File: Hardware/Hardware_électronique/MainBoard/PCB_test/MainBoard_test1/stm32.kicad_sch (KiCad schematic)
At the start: 1 part, among them U1 STM32H735IGTx

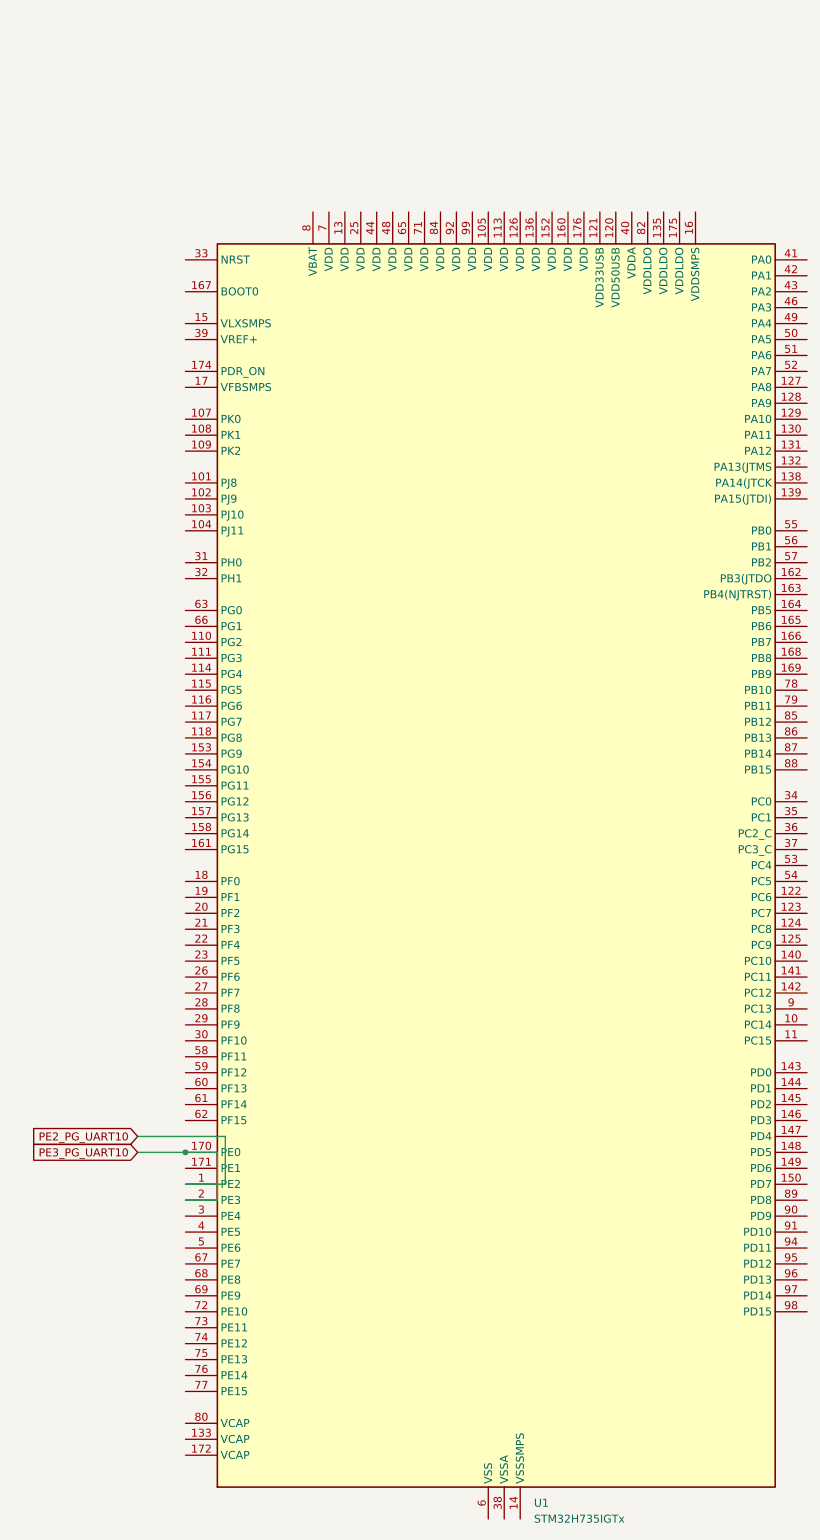
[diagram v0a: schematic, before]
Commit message: Adding motor board
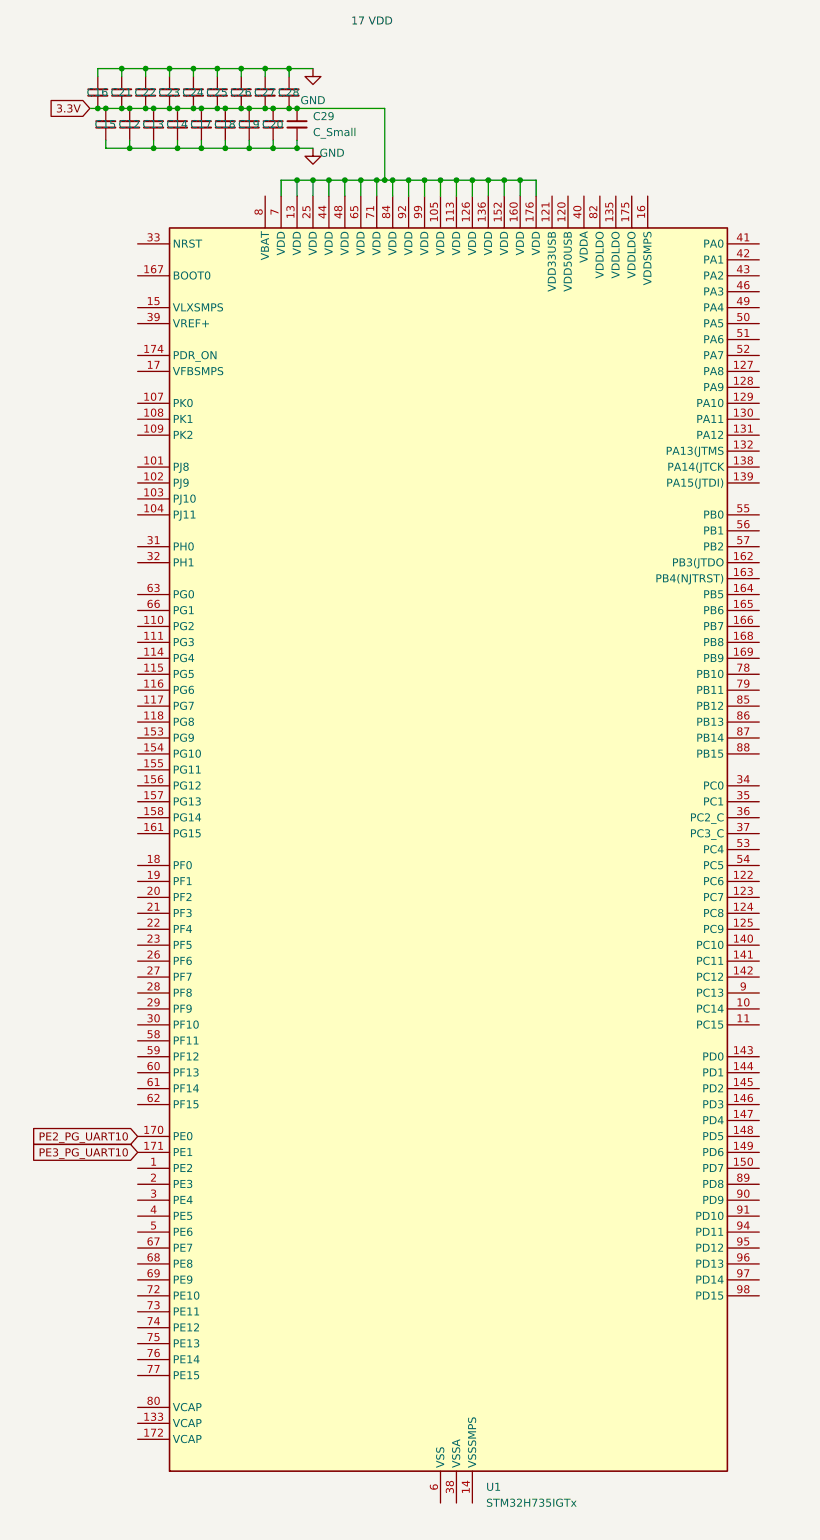
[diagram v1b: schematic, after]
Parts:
- added C12, C13, C14, C15, C16, C17, C18, C19, C20, C21, C22, C23, C24, C25, C26, C27, C28: 100n, symbol Device:C_Small
- added C29: C_Small, symbol Device:C_Small
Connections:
- net PE2_PG_UART10: now also U1.170 (PE0); no longer U1.1 (PE2)
- net PE3_PG_UART10: now also U1.171 (PE1); no longer U1.170 (PE0), U1.2 (PE3)
- net 3.3V: now reaches U1.105 (VDD)
- net 3.3V: now also U1.113 (VDD), U1.126 (VDD), U1.13 (VDD), U1.136 (VDD), U1.152 (VDD), U1.160 (VDD), U1.176 (VDD), U1.25 (VDD), U1.44 (VDD), U1.48 (VDD), U1.65 (VDD), U1.7 (VDD), U1.71 (VDD), U1.84 (VDD), U1.92 (VDD), U1.99 (VDD), C12.1, C13.1, C14.1, C15.1, C16.2, C17.1, C18.1, C19.1, C20.1, C21.2, C22.2, C23.2, C24.2, C25.2, C26.2, C27.2, C28.2, C29.1
- new net GND: C12.2, C13.2, C14.2, C15.2, C16.1, C17.2, C18.2, C19.2, C20.2, C21.1, C22.1, C23.1, C24.1, C25.1, C26.1, C27.1, C28.1, C29.2
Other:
- note added: "17 VDD"
- moved on the sheet: U1

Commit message: ey
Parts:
- added C30, C31, C32, C33: 10n, Capacitor_SMD:C_0402_1005Metric, symbol Device:C_Small
- added C34: 1u, Capacitor_SMD:C_0603_1608Metric_Pad1.08x0.95mm_HandSolder, symbol Device:C_Small
- added C35, C36: 100n, Capacitor_SMD:C_0402_1005Metric, symbol Device:C_Small
- added D18, D19, D20, D21: Blue LED, LED_SMD:LED_0603_1608Metric, symbol Device:LED
- added J2: Conn_ST_STDC14, Connector_PinHeader_1.27mm:PinHeader_2x07_P1.27mm_Vertical_SMD, symbol Connector:Conn_ST_STDC14
- added L3: 39n, Inductor_SMD:L_0603_1608Metric, symbol Device:L_Small
- added R12, R13, R14, R15, R16, R17, R18, R19: 10k, Resistor_SMD:R_0402_1005Metric, symbol Device:R_Small
- added R20, R21, R22, R23: 390, Resistor_SMD:R_0402_1005Metric, symbol Device:R_Small
- added SW1, SW2, SW3, SW4: SW_Push, Custom:435451019820, symbol Switch:SW_Push
- C29: value C_Small -> 10u
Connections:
- net GND: now also C16.2, C21.2, C22.2, C23.2, C24.2, C25.2, C26.2, C27.2, C28.2, U1.100 (VSS), U1.106 (VSS), U1.112 (VSS), U1.119 (VSS), U1.12 (VSS), U1.134 (VSS), U1.137 (VSS), U1.14 (VSSSMPS), U1.151 (VSS), U1.159 (VSS), U1.173 (VSS), U1.24 (VSS), U1.38 (VSSA), U1.45 (VSS), U1.47 (VSS), U1.6 (VSS), U1.64 (VSS), U1.70 (VSS), U1.81 (VSS), U1.83 (VSS), U1.93 (VSS), C30.1, C31.1, C32.1, C33.1, C34.2, C35.2, C36.2, J2.11 (GNDDetect), J2.5 (GND), J2.7 (GND), R20.2, R21.2, R22.2, R23.2, SW1.2, SW2.2, SW3.2, SW4.2; no longer C16.1, C21.1, C22.1, C23.1, C24.1, C25.1, C26.1, C27.1, C28.1
- net RX2: now reaches U1.148 (PD5)
- net TX2: now reaches U1.149 (PD6)
- net NRST: now reaches U1.33 (NRST)
- net NRST: now also C30.2, J2.12 (~{RST}), R12.2
- net +3.3VA: now reaches U1.40 (VDDA)
- net +3.3VA: now also C34.1, C35.1, C36.1, L3.2
- net TX3: now reaches U1.78 (PB10)
- net RX3: now reaches U1.79 (PB11)
- net +3.3V: now reaches U1.8 (VBAT)
- net +3.3V: now also C12.1, C13.1, C14.1, C15.1, C16.1, C17.1, C18.1, C19.1, C20.1, C21.1, C22.1, C23.1, C24.1, C25.1, C26.1, C27.1, C28.1, C29.1, U1.105 (VDD), U1.113 (VDD), U1.126 (VDD), U1.13 (VDD), U1.136 (VDD), U1.152 (VDD), U1.160 (VDD), U1.176 (VDD), U1.25 (VDD), U1.44 (VDD), U1.48 (VDD), U1.65 (VDD), U1.7 (VDD), U1.71 (VDD), U1.84 (VDD), U1.92 (VDD), U1.99 (VDD), J2.3 (VCC), L3.1, R16.2, R17.2, R18.2, R19.2
- net RX5: now reaches U1.85 (PB12)
- net TX5: now reaches U1.86 (PB13)
- net TX1: now reaches U1.87 (PB14)
- net RX1: now reaches U1.88 (PB15)
- removed net 3.3V: C12.1, C13.1, C14.1, C15.1, C16.2, C17.1, C18.1, C19.1, C20.1, C21.2, C22.2, C23.2, C24.2, C25.2, C26.2, C27.2, C28.2, C29.1, U1.105 (VDD), U1.113 (VDD), U1.126 (VDD), U1.13 (VDD), U1.136 (VDD), U1.152 (VDD), U1.160 (VDD), U1.176 (VDD), U1.25 (VDD), U1.44 (VDD), U1.48 (VDD), U1.65 (VDD), U1.7 (VDD), U1.71 (VDD), U1.84 (VDD), U1.92 (VDD), U1.99 (VDD)
- new net: R14.1, R18.1, SW3.1
- new net: D20.1 (K), R22.1
- new net: D21.1 (K), R23.1
- new net: R13.1, R17.1, SW2.1
- new net: R12.1, R16.1, SW1.1
- new net: D18.1 (K), R20.1
- new net: R15.1, R19.1, SW4.1
- new net: D19.1 (K), R21.1
- new net SWCLK: J2.6 (JCLK/SWCLK)
- new net SWDIO: J2.4 (JTMS/SWDIO)
- new net SWO: J2.8 (JTDO/SWO)
- new net USR_BTN_1: C31.2, R13.2
- new net USR_BTN_2: C32.2, R14.2
- new net USR_BTN_3: C33.2, R15.2
- new net USR_LED_1: D18.2 (A)
- new net USR_LED_2: D19.2 (A)
- new net USR_LED_3: D20.2 (A)
- new net USR_LED_4: D21.2 (A)
- new net VCP_RX: J2.13 (VCP_RX)
- new net VCP_TX: J2.14 (VCP_TX)
- no-connect marks 0 -> 16
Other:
- note added: "Buttons Configure uC for pull-up on user buttons"
- note added: "LEDS"
- note added: "ST-Link"
- moved on the sheet: C12, C13, C14, C15, C17, C18, C19, C20, C29

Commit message: commitment
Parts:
- added C37: 10u, Capacitor_SMD:C_0603_1608Metric_Pad1.08x0.95mm_HandSolder, symbol Device:C_Polarized
- added C38: 22u, Capacitor_SMD:C_0603_1608Metric_Pad1.08x0.95mm_HandSolder, symbol Device:C_Polarized
- added C39: 100n, Capacitor_SMD:C_0402_1005Metric, symbol Device:C_Small
- added D1, D2, D3, D4, D5, D6, D7, D8, D9: ESD7C5.0DT5G, Package_TO_SOT_SMD:SOT-416, symbol Power_Protection:RCLAMP0582B
- added LIDAR1, UART1, UART2, UART3, UART4, UART5, UART6, UART7, UART8: Conn_01x04_Male, Connector_JST:JST_XH_B4B-XH-A_1x04_P2.50mm_Vertical, symbol Connector:Conn_01x04_Male
- added TP2, TP5: TestPoint, TestPoint:TestPoint_Pad_D2.0mm, symbol Connector:TestPoint
- added U4: AZ1117-3.3, Package_TO_SOT_SMD:SOT-223-3_TabPin2, symbol Regulator_Linear:AZ1117-3.3
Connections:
- net +3.3V: now also C38.1, TP5.1, U4.2 (VO)
- net +3.3VA: now also U1.39 (VREF+)
- net GND: now also C37.2, C38.2, C39.1, D1.3 (A), D2.3 (A), D3.3 (A), D4.3 (A), D5.3 (A), D6.3 (A), D7.3 (A), D8.3 (A), D9.3 (A), LIDAR1.4 (Pin_4), U4.1 (GND), UART1.4 (Pin_4), UART2.4 (Pin_4), UART3.4 (Pin_4), UART4.4 (Pin_4), UART5.4 (Pin_4), UART6.4 (Pin_4), UART7.4 (Pin_4), UART8.4 (Pin_4)
- net NRST: now also C39.2
- net RX1: now also D1.2 (K2), UART1.3 (Pin_3)
- net RX2: now also D5.2 (K2), UART5.3 (Pin_3)
- net RX3: now also D2.2 (K2), UART2.3 (Pin_3)
- net RX5: now also D4.2 (K2), UART4.3 (Pin_3)
- net TX1: now also D1.1 (K1), UART1.2 (Pin_2)
- net TX2: now also D5.1 (K1), UART5.2 (Pin_2)
- net TX3: now also D2.1 (K1), UART2.2 (Pin_2)
- net TX5: now also D4.1 (K1), UART4.2 (Pin_2)
- net RXtoRPI: now reaches U1.1 (PE2)
- net TX8: now reaches U1.101 (PJ8)
- net TX8: now also D8.1 (K1), UART8.2 (Pin_2)
- net RX8: now reaches U1.102 (PJ9)
- net RX8: now also D8.2 (K2), UART8.3 (Pin_3)
- net TX6: now reaches U1.122 (PC6)
- net TX6: now also D6.1 (K1), UART6.2 (Pin_2)
- net RX6: now reaches U1.123 (PC7)
- net RX6: now also D6.2 (K2), UART6.3 (Pin_3)
- net RX4: now reaches U1.130 (PA11)
- net RX4: now also D3.2 (K2), UART3.3 (Pin_3)
- net TX4: now reaches U1.131 (PA12)
- net TX4: now also D3.1 (K1), UART3.2 (Pin_2)
- net TXtoRPI: now reaches U1.2 (PE3)
- net RX7: now reaches U1.67 (PE7)
- net RX7: now also D7.2 (K2), UART7.3 (Pin_3)
- net TX7: now reaches U1.68 (PE8)
- net TX7: now also D7.1 (K1), UART7.2 (Pin_2)
- net RX_Lidar: now reaches U1.97 (PD14)
- net RX_Lidar: now also D9.2 (K2), LIDAR1.3 (Pin_3)
- net TX_Lidar: now reaches U1.98 (PD15)
- net TX_Lidar: now also D9.1 (K1), LIDAR1.2 (Pin_2)
- net PE2_PG_UART10: no longer names the net of U1.170 (PE0)
- net PE3_PG_UART10: no longer names the net of U1.171 (PE1)
- new net +5V: C37.1, TP2.1, U4.3 (VI)
- new net VBUS: LIDAR1.1 (Pin_1), UART1.1 (Pin_1), UART2.1 (Pin_1), UART3.1 (Pin_1), UART4.1 (Pin_1), UART5.1 (Pin_1), UART6.1 (Pin_1), UART7.1 (Pin_1), UART8.1 (Pin_1)
- no-connect marks 16 -> 13
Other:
- moved on the sheet: C12, C13, C14, C15, C16, C17, C18, C19, C20, C21, C22, C23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

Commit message: hey
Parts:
- added C40: 100n, symbol Device:C_Small
- added C41: 100n, Capacitor_SMD:C_0402_1005Metric, symbol Device:C_Small
- added C42, C43, C44: 2.2u, symbol Device:C_Small
- added C45, C46, C47: 1u, Capacitor_SMD:C_0603_1608Metric_Pad1.08x0.95mm_HandSolder, symbol Device:C_Small
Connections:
- net USR_BTN_3 is gone; now on net BOOT0: C33.2, R15.2
- net +3.3V: now also U1.121 (VDD33USB), U1.135 (VDDLDO), U1.175 (VDDLDO), U1.82 (VDDLDO), C40.1, C45.1, C46.1, C47.1
- net +5V: now also U1.120 (VDD50USB), C41.1
- net GND: now also C40.2, C41.2, C42.2, C43.2, C44.2, C45.2, C46.2, C47.2
- net SWCLK: now also U1.138 (PA14(JTCK)
- net SWDIO: now also U1.132 (PA13(JTMS)
- net SWO: now also U1.162 (PB3(JTDO)
- net USR_BTN_1: now also U1.163 (PB4(NJTRST))
- net USR_BTN_2: now also U1.164 (PB5)
- net at U1.133 (VCAP): now also C43.1
- net BOOT0: now reaches U1.167 (BOOT0)
- net at U1.172 (VCAP): now also C44.1
- net at U1.80 (VCAP): now also C42.1
- no-connect marks 13 -> 100
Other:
- note added: "Checker boot0"

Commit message: approaching end of schematics
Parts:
- added D22: ESD7C5.0DT5G, Package_TO_SOT_SMD:SOT-416, symbol Power_Protection:RCLAMP0582B
- added J3: USB_A, symbol Connector:USB_A
- added UART9: Conn_01x04_Male, Connector_JST:JST_XH_B4B-XH-A_1x04_P2.50mm_Vertical, symbol Connector:Conn_01x04_Male
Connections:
- net GND: now also U1.174 (PDR_ON), D22.3 (A), J3.4 (GND), J3.5 (Shield), UART9.4 (Pin_4)
- net RX2: now also U1.149 (PD6); no longer U1.148 (PD5)
- net RX4: now also U1.42 (PA1), D22.2 (K2), UART9.3 (Pin_3); no longer D3.2 (K2), U1.130 (PA11), UART3.3 (Pin_3)
- net RXtoRPI: now also U1.128 (PA9); no longer U1.1 (PE2)
- net TX2: now also U1.148 (PD5); no longer U1.149 (PD6)
- net TX4: now also U1.41 (PA0), D22.1 (K1), UART9.2 (Pin_2); no longer D3.1 (K1), U1.131 (PA12), UART3.2 (Pin_2)
- net TXtoRPI: now also U1.129 (PA10); no longer U1.2 (PE3)
- net USR_LED_1: now also U1.18 (PF0)
- net USR_LED_2: now also U1.19 (PF1)
- net USR_LED_3: now also U1.20 (PF2)
- net USR_LED_4: now also U1.21 (PF3)
- net VBUS: now also UART9.1 (Pin_1)
- net VCP_RX: no longer names the net of J2.13 (VCP_RX)
- net VCP_TX: no longer names the net of J2.14 (VCP_TX)
- new net RX10: D3.2 (K2), U1.1 (PE2), UART3.3 (Pin_3)
- new net TX10: D3.1 (K1), U1.2 (PE3), UART3.2 (Pin_2)
- new net USB_DM: J3.2 (D-), U1.131 (PA12)
- new net USB_DP: J3.3 (D+), U1.130 (PA11)
- no-connect marks 100 -> 96
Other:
- note added: "LDO +5V-> +3.3V"
- note removed: "Checker boot0"
- moved on the sheet: C37, C38, TP2, TP5, U4

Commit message: quite finished schematics
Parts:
- added J4: Conn_01x04_Socket, Connector_JST:JST_XH_B4B-XH-A_1x04_P2.50mm_Vertical, symbol Connector:Conn_01x04_Socket

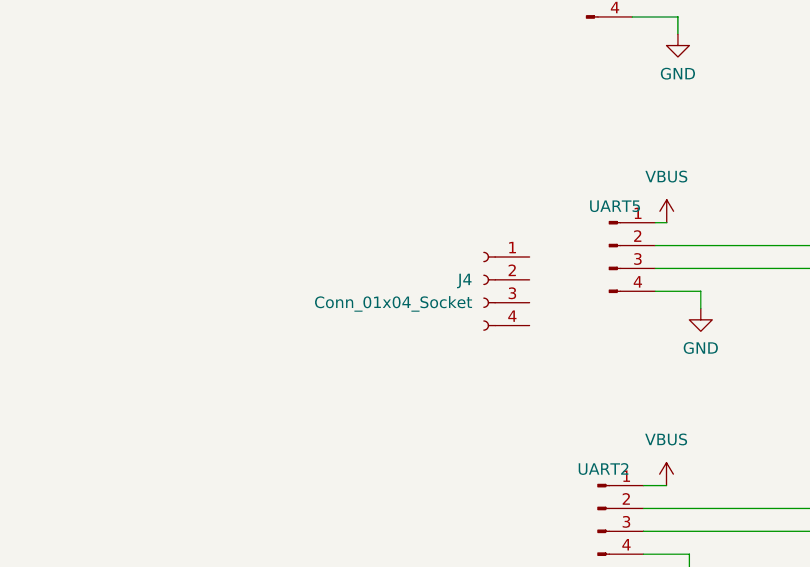
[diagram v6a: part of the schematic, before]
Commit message: finished schematics missing footprints
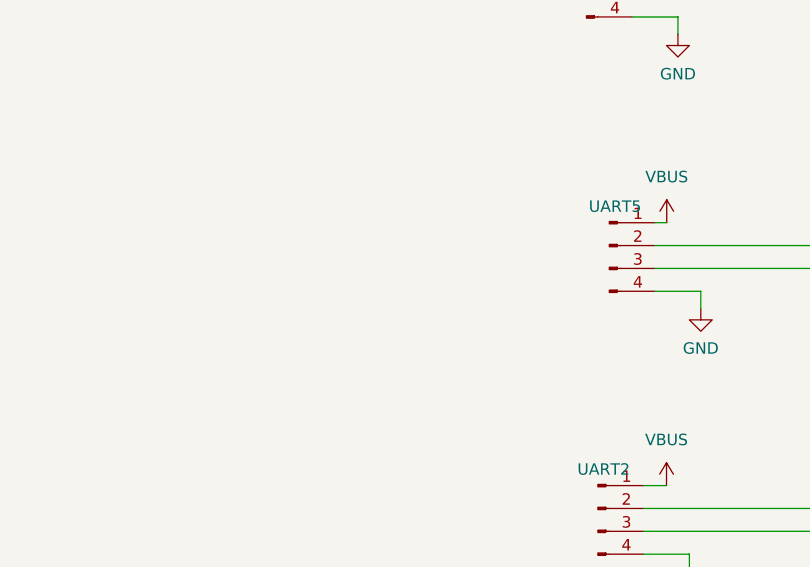
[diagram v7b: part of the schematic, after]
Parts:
- removed J4: Conn_01x04_Socket, Connector_JST:JST_XH_B4B-XH-A_1x04_P2.50mm_Vertical, symbol Connector:Conn_01x04_Socket

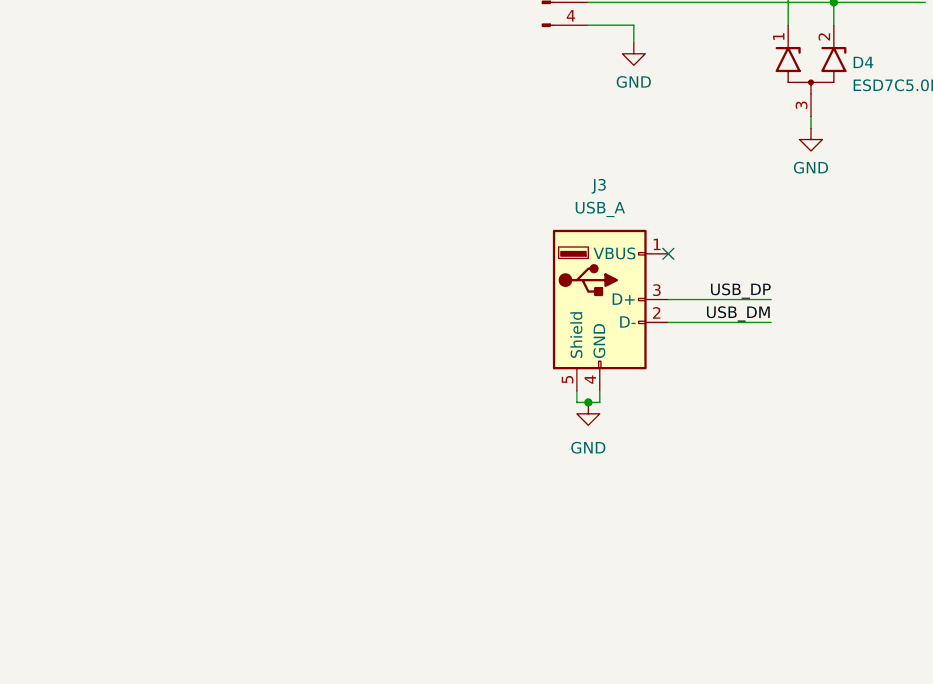
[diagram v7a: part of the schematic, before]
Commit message: beginning of PCB design with Rpi4 shield shape
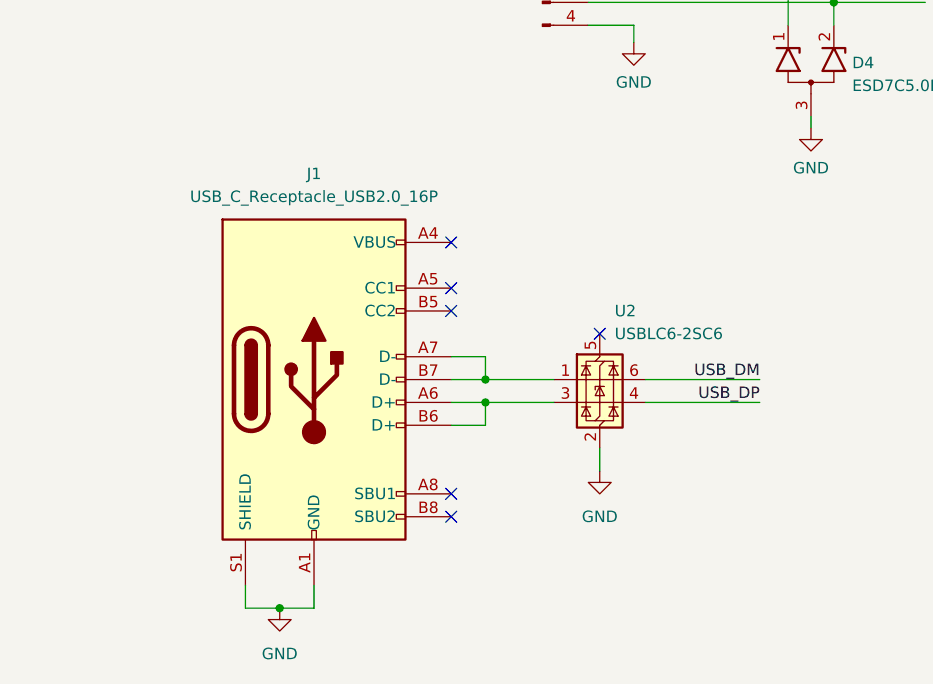
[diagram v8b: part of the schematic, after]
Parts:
- removed J3: USB_A, symbol Connector:USB_A
- added J1: USB_C_Receptacle_USB2.0_16P, Connector_USB:USB_C_Receptacle_GCT_USB4110, symbol Connector:USB_C_Receptacle_USB2.0_16P
- added U2: USBLC6-2SC6, Package_TO_SOT_SMD:SOT-23-6, symbol Power_Protection:USBLC6-2SC6
- C12, C13, C14, C15, C16, C17, C18, C19, C20, C21, C22, C23, C24, C25, C26, C27, C28, C40, C42, C43, C44: footprint (none) -> Capacitor_SMD:C_0402_1005Metric_Pad0.74x0.62mm_HandSolder
- C29: footprint (none) -> Capacitor_SMD:C_0603_1608Metric_Pad1.08x0.95mm_HandSolder
- C37, C38: footprint Capacitor_SMD:C_0603_1608Metric_Pad1.08x0.95mm_HandSolder -> Capacitor_SMD:C_0805_2012Metric_Pad1.18x1.45mm_HandSolder
- SW1, SW2, SW3, SW4: footprint Custom:435451019820 -> MainBoard:435451019820
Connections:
- net GND: now also J1.A1 (GND), J1.A12 (GND), J1.B1 (GND), J1.B12 (GND), J1.S1 (SHIELD), U2.2 (GND)
- net USB_DM: now also U2.6 (I/O1)
- net USB_DP: now also U2.4 (I/O2)
- new net: J1.A7 (D-), J1.B7 (D-), U2.1 (I/O1)
- new net: J1.A6 (D+), J1.B6 (D+), U2.3 (I/O2)
- new net: J1.A4 (VBUS), J1.A9 (VBUS), J1.B4 (VBUS), J1.B9 (VBUS)
- no-connect marks 96 -> 101
